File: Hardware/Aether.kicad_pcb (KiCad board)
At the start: 2 copper layers, 70 parts, among them J1 PRGM, Q1 IRLML6401, U1 ANTENOVA-UB, U2 ADF7012, U3 AAT1217, U4 MCP6L02T, U5 MSP430G2553-PW28, X1 VCXO, X2 CRYSTAL

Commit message: RF routing
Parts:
- moved C17 2.92 mm to (174.0, 108.5), turned to 270 degrees
- moved C13 2.50 mm to (187.0, 106.0)
- moved C15 2.50 mm to (174.0, 106.0)
- moved C16 2.50 mm to (172.5, 106.0)
- moved R5 2.50 mm to (187.0, 108.5)
- moved R7 1.50 mm to (175.5, 106.0)
- moved C23 1.25 mm to (188.8, 100.5)
- moved L7 1.00 mm to (187.5, 102.0)
- moved C3 0.81 mm to (137.7, 102.9)
- moved C22 0.75 mm to (186.2, 100.5)
- moved L4 0.75 mm to (178.8, 100.5)
- moved L1 0.50 mm to (121.5, 110.0)
- moved L5 0.50 mm to (180.0, 102.0)
- moved L6 0.50 mm to (185.0, 102.0)
- moved C6 0.40 mm to (139.6, 115.0)
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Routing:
- net GND: track 0.00 -> 27.6 mm, vias 0 -> 8
- net +3.3V: track 2.18 -> 19.4 mm
- net /Transmitter/CPOut: track 0.00 -> 12.0 mm
- net N-0000035: track 0.00 -> 10.8 mm
- net N-0000050: track 0.00 -> 8.46 mm
- net /Transmitter/VCOIn: track 0.00 -> 8.35 mm, vias 0 -> 2
- net N-0000049: track 0.00 -> 4.92 mm
- net N-0000048: track 0.00 -> 4.13 mm
- net N-0000047: track 0.00 -> 4.01 mm
- net N-0000037: track 0.00 -> 2.92 mm
- net N-0000036: track 0.00 -> 2.92 mm
- net N-0000055: track 0.00 -> 2.90 mm
- net N-0000054: track 0.00 -> 2.90 mm
- net /Transmitter/L2: track 0.00 -> 2.18 mm
- net /Transmitter/L1: track 0.00 -> 2.18 mm
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
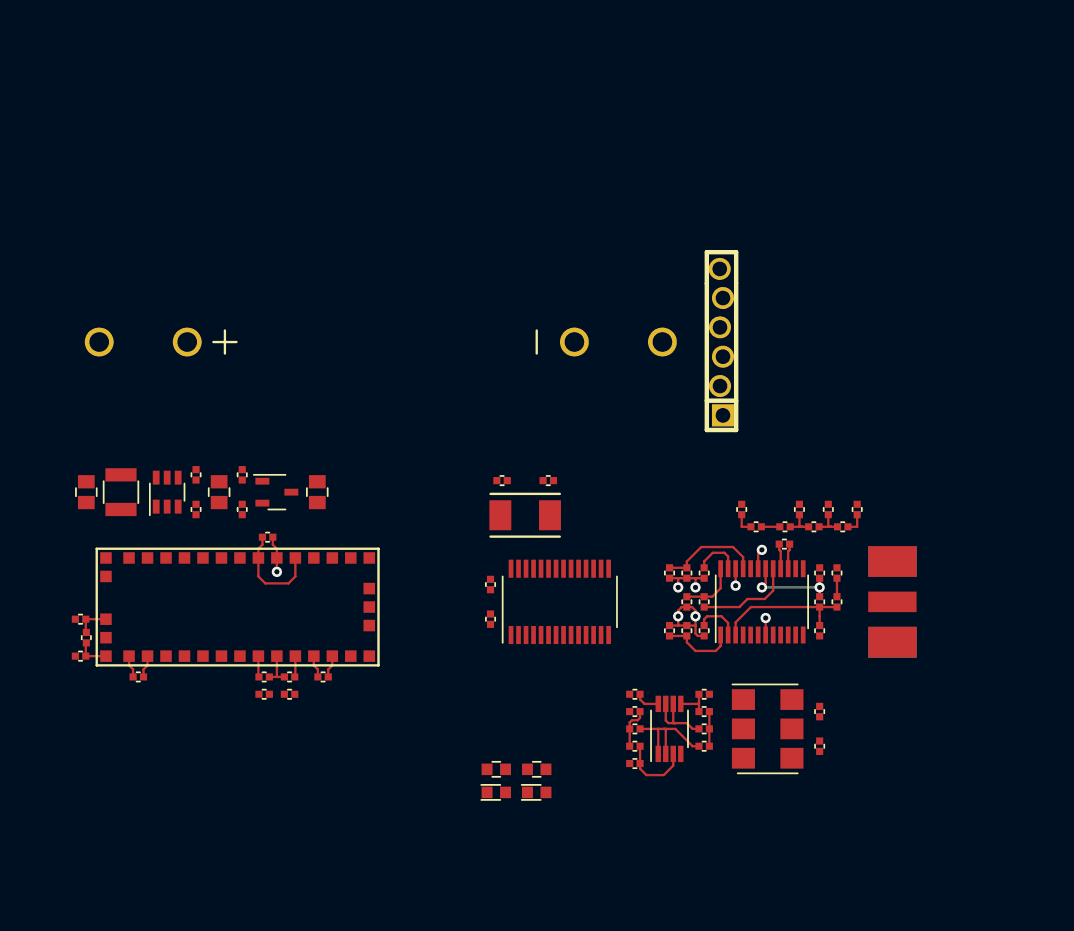
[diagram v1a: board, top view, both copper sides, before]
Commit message: Add expansion headers
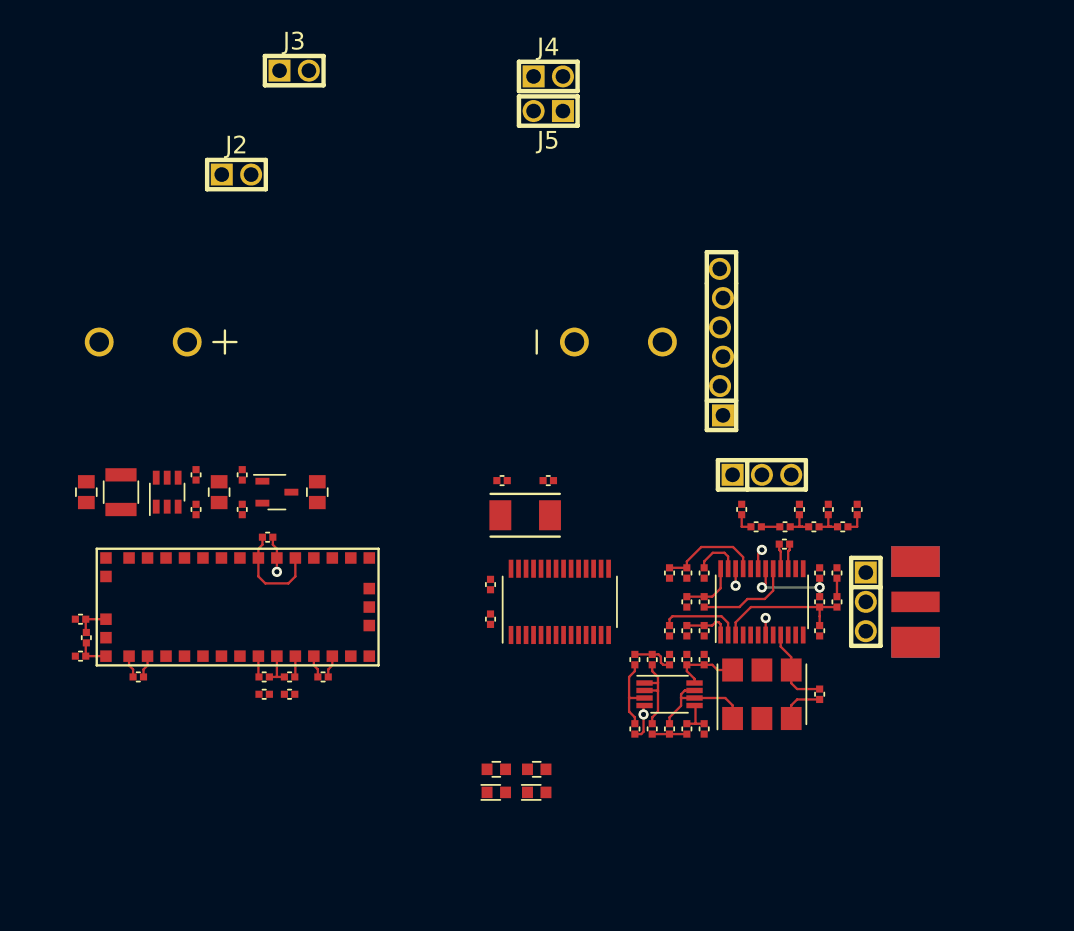
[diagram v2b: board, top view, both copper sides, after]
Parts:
- added J2: CONN-2, HDRV2W38P254_2X1, F.Cu at (135.0, 71.5)
- added J3: CONN-2, HDRV2W38P254_2X1, F.Cu at (140.0, 62.5)
- added J4: CONN-2, HDRV2W38P254_2X1, F.Cu at (162.0, 63.0)
- added J5: CONN-2, HDRV2W38P254_2X1, F.Cu at (162.0, 66.0)
- added J6: CONN-3, HDRV3W38P254_3X1, F.Cu at (180.5, 97.5)
- added J7: CONN-3, HDRV3W38P254_3X1, F.Cu at (189.5, 108.5)
- moved C8 11.0 mm to (175.5, 113.5)
- moved R10 7.50 mm to (169.5, 113.5), turned to 270 degrees
- moved C25 6.18 mm to (171.0, 113.5), turned to 270 degrees
- moved C26 5.41 mm to (174.0, 113.5), turned to 90 degrees
- moved R8 5.41 mm to (172.5, 113.5), turned to 270 degrees
- moved R11 4.74 mm to (171.0, 119.5), turned to 270 degrees
- moved C9 4.50 mm to (185.5, 116.5), turned to 270 degrees
- moved X1 3.04 mm to (180.5, 116.5), turned to 0 degrees
- moved C19 3.00 mm to (172.5, 111.0)
- moved C27 3.00 mm to (169.5, 119.5), turned to 270 degrees
- moved C30 3.00 mm to (172.5, 119.5), turned to 90 degrees
- moved C32 3.00 mm to (175.5, 119.5), turned to 270 degrees
- moved U4 3.00 mm to (172.5, 116.5), turned to 270 degrees
- moved R12 2.12 mm to (174.0, 119.5), turned to 90 degrees
- moved AE1 2.00 mm to (196.0, 108.5)
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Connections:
- AE1 pad P: /Transmitter/RFOut -> N-0000019
- L4 pad 2: (no net) -> +3.3V
- U5 pad 22: (no net) -> /Core/SCL
- X1 pad 2: /Core/TX_En -> (no net)
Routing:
- net N-0000058: track 0.00 -> 7.22 mm
- net GND: track 27.6 -> 21.8 mm, vias 8 -> 5
- net /Core/Mod: track 6.45 -> 10.2 mm
- net N-0000055: track 4.01 -> 7.01 mm
- net N-0000093: track 10.3 -> 7.94 mm
- net +3.3V: track 19.4 -> 20.8 mm
- net N-0000074: track 6.40 -> 6.92 mm

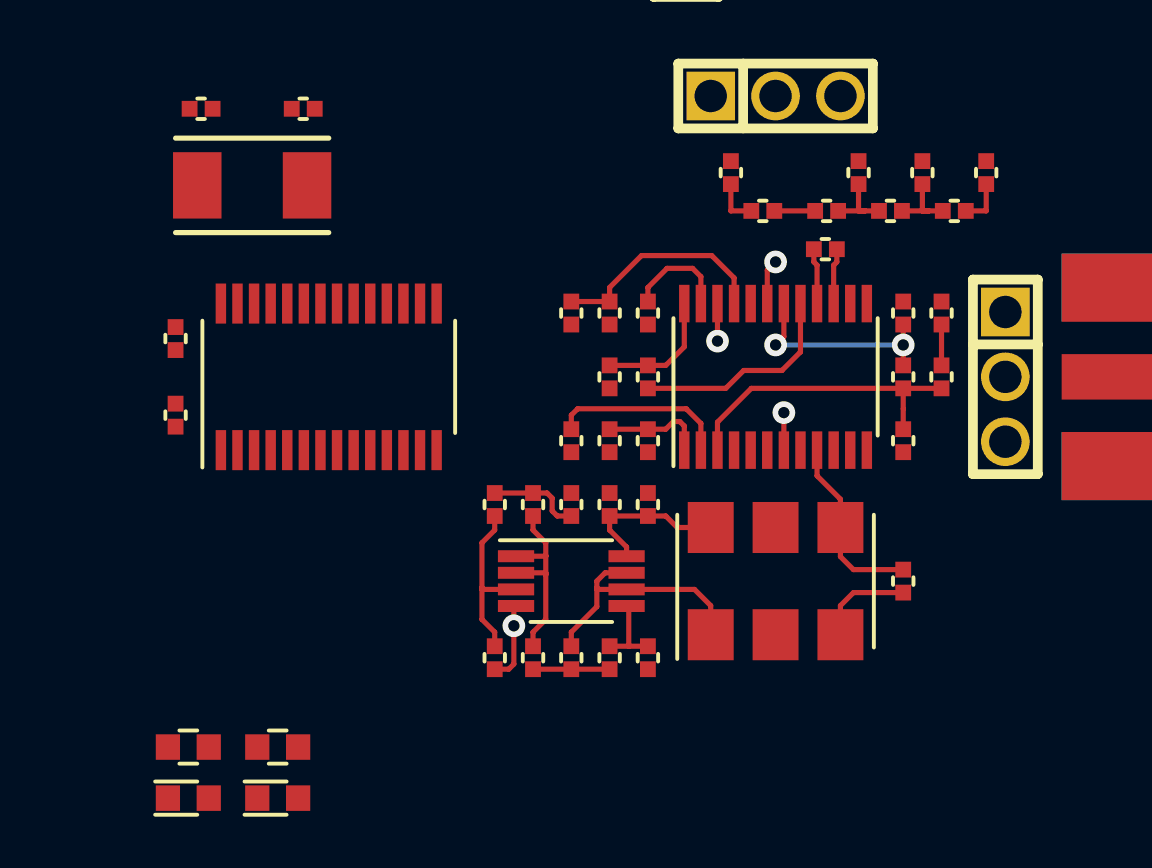
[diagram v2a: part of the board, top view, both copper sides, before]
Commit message: Change to soft SPI, routing
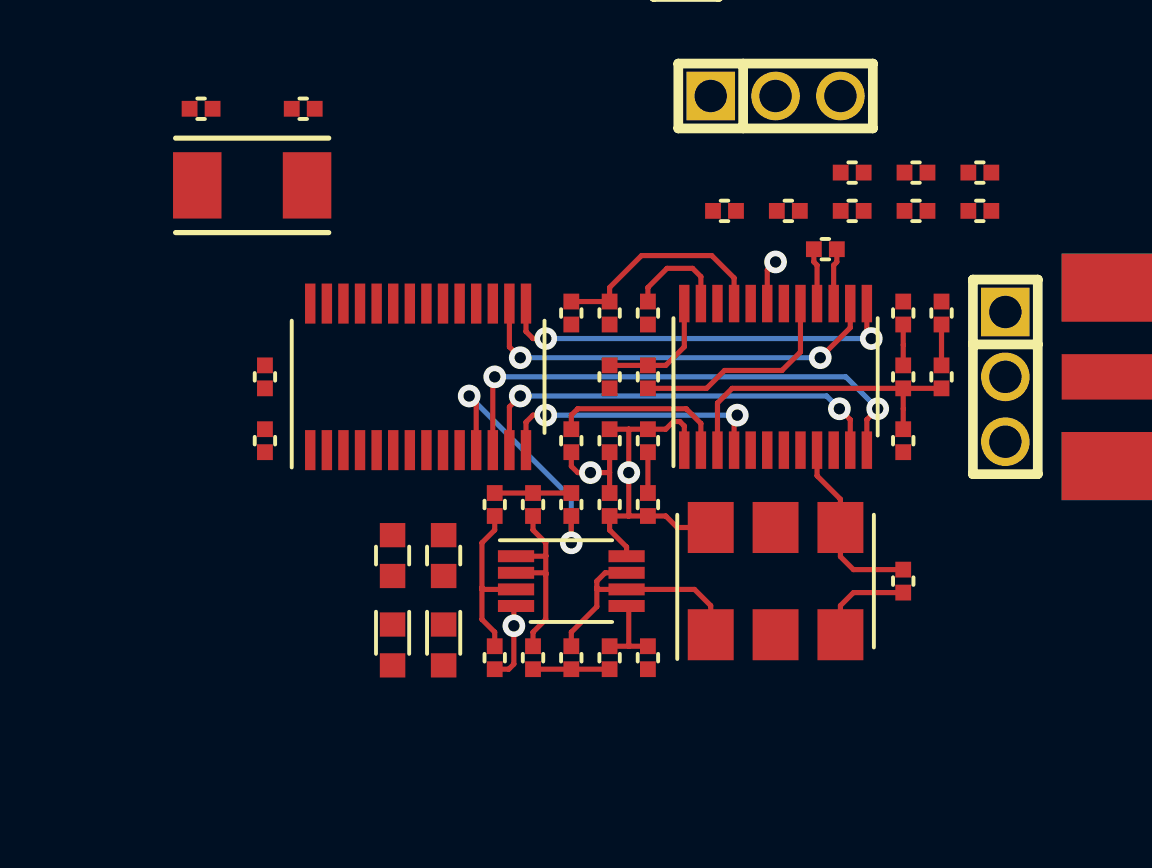
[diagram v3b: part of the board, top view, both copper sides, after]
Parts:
- moved R1 12.5 mm to (167.5, 115.5), turned to 90 degrees
- moved D1 11.7 mm to (167.5, 119.0), turned to 90 degrees
- moved R2 8.75 mm to (165.5, 115.5), turned to 90 degrees
- moved D2 7.50 mm to (165.5, 119.0), turned to 90 degrees
- moved R13 3.81 mm to (160.5, 108.5)
- moved C34 3.64 mm to (160.5, 111.0), turned to 270 degrees
- moved U5 3.50 mm to (166.5, 108.5)
- moved L4 1.52 mm to (178.5, 102.0), turned to 180 degrees
- moved C20 1.00 mm to (183.5, 102.0)
- moved L5 1.00 mm to (181.0, 102.0)
- moved L6 1.00 mm to (186.0, 102.0)
- moved L7 1.00 mm to (188.5, 102.0)
- moved C21 0.25 mm to (183.5, 100.5), turned to 180 degrees
- moved C22 0.25 mm to (186.0, 100.5), turned to 180 degrees
- moved C23 0.25 mm to (188.5, 100.5), turned to 180 degrees
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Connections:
- J1 pad 3: (no net) -> +5V
- J5 pad 1: /Core/SCL -> /Core/SDA
- J5 pad 2: /Core/DATA -> /Core/SCL
- R1 pad 2: (no net) -> /Core/Stat
- R8 pad 1: (no net) -> /Core/AF
- U1 pad 9: (no net) -> /Core/GPS_Perf
- U2 pad 12: /Core/DATA -> /Core/MOSI
- U2 pad 4: (no net) -> /Core/TXD
- U5 pad 10: (no net) -> /Core/CLK_En
- U5 pad 11: (no net) -> /Core/AF
- U5 pad 12: (no net) -> /Core/MOSI
- U5 pad 13: (no net) -> /Core/SCK
- U5 pad 14: (no net) -> /Core/TXD
- U5 pad 15: (no net) -> /Core/SS
- U5 pad 16: (no net) -> /Core/TX_En
- U5 pad 21: (no net) -> +5V
- U5 pad 23: /Core/DATA -> /Core/SDA
- U5 pad 6: /Core/SS -> (no net)
- U5 pad 7: /Core/SCK -> /Core/Stat
- U5 pad 8: (no net) -> /Core/GPS_Perf
- U5 pad 9: (no net) -> /Core/GPS_En
- X1 pad 2: (no net) -> /Core/CLK_En
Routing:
- net /Core/MOSI: track 0.00 -> 20.2 mm, vias 0 -> 2
- net /Core/SCK: track 0.00 -> 16.8 mm, vias 0 -> 2
- net /Core/TX_En: track 0.00 -> 16.7 mm, vias 0 -> 2
- net /Core/SS: track 0.00 -> 16.2 mm, vias 0 -> 2
- net /Core/TXD: track 0.00 -> 10.9 mm, vias 0 -> 2
- net /Core/AF: track 0.00 -> 10.7 mm, vias 0 -> 2
- net /Transmitter/VCOIn: track 8.35 -> 1.60 mm, vias 2 -> 0
- net +3.3V: track 20.8 -> 24.2 mm, vias 0 -> 1
- net N-0000062: track 2.90 -> 0.00 mm
- net N-0000061: track 2.90 -> 0.00 mm
- net GND: track 21.8 -> 24.2 mm, vias 5 -> 4
- net /Transmitter/RFOut: track 1.85 -> 0.00 mm
- net /Transmitter/RF: track 1.85 -> 0.00 mm
- net N-0000063: track 1.60 -> 0.00 mm
- net N-0000079: track 3.67 -> 3.00 mm

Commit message: Additional layout
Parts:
- added R14: 10k, RESC1005-N, F.Cu at (172.5, 102.0)
- B1: footprint BATT-AA-BK92 -> BATT-AA-BK53; moved to B.Cu
- X2: value CRYSTAL -> 8MHz; footprint XTAL-2SMD-60x35 -> XTAL-2SMD-50X32
- moved B1 52.8 mm to (173.5, 132.0)
- moved J5 34.3 mm to (169.5, 99.5), turned to 0 degrees
- moved C1 29.3 mm to (137.5, 128.0)
- moved C24 29.3 mm to (117.5, 128.0)
- moved C28 29.3 mm to (127.0, 129.5)
- moved C29 29.3 mm to (129.0, 128.0)
- moved L8 29.3 mm to (120.5, 128.0)
- moved Q1 29.3 mm to (134.0, 128.0)
- moved R3 29.3 mm to (131.0, 129.5)
- moved R4 29.3 mm to (131.0, 126.5)
- moved R9 29.3 mm to (127.0, 126.5)
- moved U3 29.3 mm to (124.5, 128.0)
- moved J6 6.80 mm to (187.0, 99.5)
- moved J1 5.88 mm to (178.2, 91.8), turned to 180 degrees
- moved C31 4.03 mm to (162.0, 98.5), turned to 180 degrees
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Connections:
- J2 pad 1: (no net) -> +BATT
- J2 pad 2: (no net) -> GND
- J6 pad 1: (no net) -> +BATT
- U5 pad 21: +5V -> N-0000068
- U5 pad 7: /Core/Stat -> /Core/GPS_Perf
- U5 pad 8: /Core/GPS_Perf -> /Core/GPS_En
- U5 pad 9: /Core/GPS_En -> /Core/Stat
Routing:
- net N-0000040: track 10.8 -> 0.00 mm
- net /Core/XOut: track 0.00 -> 9.03 mm
- net /Core/XIn: track 0.00 -> 9.03 mm
- net /Transmitter/VCOIn: track 1.60 -> 9.15 mm, vias 0 -> 2
- net GND: track 24.2 -> 20.0 mm
- net /Core/Stat: track 0.00 -> 3.34 mm
- net N-0000041: track 2.92 -> 0.00 mm
- net N-0000039: track 2.92 -> 0.00 mm
- net N-0000026: track 0.00 -> 1.90 mm
- net N-0000025: track 0.00 -> 1.90 mm
- net N-0000045: track 1.82 -> 0.00 mm
- net N-0000044: track 1.82 -> 0.00 mm
- net /Core/CLK_En: track 0.00 -> 1.79 mm, vias 0 -> 1
- net +3.3V: track 24.2 -> 23.6 mm

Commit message: Additional layout
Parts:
- added C35: 4.7uF, CAPC2012-N, F.Cu at (174.0, 103.5)
- C10: value C -> 0.1uF
- C11, C15: value C -> 5.1pF
- C12: value C -> 1200pF
- C13: value C -> 0.018uF
- C14: value C -> 560pF
- C16: value C -> 10nF
- C17: value C -> 0.47uF
- C18: value C -> 0.022uF
- C19: value C -> 1uF
- C20: value C -> 470pF
- C21, C23: value C -> 3.3pF
- C22: value C -> 8.2pF
- C31, C33: value C -> 22pF
- D1: value LED -> STAT
- D2: value LED -> PWR
- L3: value L -> 19.2nH
- L4, L6, L7: value L -> 22nH
- L5: value L -> 10pF
- R1, R2: value R -> 120
- R5: value R -> 820
- R6: value R -> 1.6k
- R7: value R -> 3.6k
- moved J1 29.0 mm to (158.0, 112.5), turned to 270 degrees
- moved C2 16.9 mm to (132.0, 99.0)
- moved C3 16.9 mm to (143.2, 86.9)
- moved C4 16.9 mm to (142.9, 99.0)
- moved C5 16.9 mm to (148.0, 99.0)
- moved C6 16.9 mm to (145.1, 99.0)
- moved C7 16.9 mm to (127.5, 95.6)
- moved FB1 16.9 mm to (142.9, 100.5)
- moved FB2 16.9 mm to (145.1, 100.5)
- moved L1 16.9 mm to (127.0, 94.0)
- moved L2 16.9 mm to (127.0, 97.2)
- moved U1 16.9 mm to (128.5, 88.0)
- moved J6 7.50 mm to (179.5, 99.5)
- moved R14 4.07 mm to (168.5, 102.8)
- moved C21 3.26 mm to (184.5, 100.2), turned to 90 degrees
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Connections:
- U5 pad 10: /Core/CLK_En -> /Core/AF
- U5 pad 11: /Core/AF -> /Core/CLK_En
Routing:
- net GND: track 20.0 -> 35.4 mm, vias 4 -> 6
- net /Transmitter/RF: track 0.00 -> 5.26 mm
- net /Transmitter/RFOut: track 0.00 -> 4.56 mm
- net N-0000017: track 0.00 -> 3.80 mm
- net N-0000048: track 0.00 -> 2.90 mm
- net N-0000047: track 0.00 -> 2.90 mm
- net /Core/AF: track 10.7 -> 8.31 mm
- net N-0000049: track 0.00 -> 1.60 mm
- net +3.3V: track 23.6 -> 24.2 mm

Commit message: RF layout
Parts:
- B1: footprint BATT-AA-BK53 -> BATT-AA-BK92
- moved J4 54.5 mm to (162.5, 117.5), turned to 270 degrees
- moved C1 33.6 mm to (154.5, 99.0)
- moved C24 33.6 mm to (134.5, 99.0)
- moved C28 33.6 mm to (144.0, 100.5)
- moved C29 33.6 mm to (146.0, 99.0)
- moved L8 33.6 mm to (137.5, 99.0)
- moved Q1 33.6 mm to (151.0, 99.0)
- moved R3 33.6 mm to (148.0, 100.5)
- moved R4 33.6 mm to (148.0, 97.5)
- moved R9 33.6 mm to (144.0, 97.5)
- moved U3 33.6 mm to (141.5, 99.0)
- moved B1 26.9 mm to (168.5, 103.5)
- moved C5 20.9 mm to (152.0, 119.5), turned to 0 degrees
- moved C2 20.7 mm to (134.5, 119.5)
- moved C3 20.7 mm to (145.7, 107.4)
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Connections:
- U5 pad 15: /Core/SS -> /Core/TX_En
- U5 pad 16: /Core/TX_En -> /Core/SS
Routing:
- net GND: track 35.4 -> 93.9 mm, vias 6 -> 20
- net /Core/RX: track 0.00 -> 18.5 mm, vias 0 -> 1
- net +3.3V: track 24.2 -> 33.8 mm
- net /GPS/RX: track 0.00 -> 9.24 mm, vias 0 -> 1
- net /Core/SCL: track 0.00 -> 9.03 mm
- net /Core/SDA: track 0.00 -> 8.25 mm
- net /Core/TX_En: track 16.7 -> 24.9 mm
- net N-0000049: track 1.60 -> 8.31 mm
- net N-0000040: track 0.00 -> 3.89 mm
- net N-0000045: track 0.00 -> 3.12 mm
- net N-0000044: track 0.00 -> 3.12 mm
- net N-0000041: track 0.00 -> 2.92 mm
- net N-0000039: track 0.00 -> 2.92 mm
- net /Core/SS: track 16.7 -> 18.6 mm
- net /Transmitter/RF: track 5.26 -> 6.26 mm
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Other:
- net class Default: via_dia 0.889 -> 0.762; via_drill 0.635 -> 0.381
- rule via_min_drill: 0.508 -> 0.3302
- rule via_min_size: 0.889 -> 0.6858

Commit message: Board configuration
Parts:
- moved J3 40.2 mm to (158.0, 98.5), turned to 270 degrees
- moved J2 19.7 mm to (130.5, 105.5), turned to 270 degrees
- moved R14 15.6 mm to (160.5, 114.0), turned to 90 degrees
- moved C29 11.2 mm to (138.8, 107.5), turned to 180 degrees
- moved C1 9.91 mm to (149.4, 107.5), turned to 0 degrees
- moved R9 8.94 mm to (140.0, 105.5), turned to 180 degrees
- moved C28 8.20 mm to (137.5, 105.5), turned to 180 degrees
- moved Q1 5.41 mm to (148.0, 103.5), turned to 180 degrees
- moved C24 4.93 mm to (138.8, 96.5), turned to 180 degrees
- moved U3 4.85 mm to (138.8, 103.0), turned to 270 degrees
- moved R4 3.02 mm to (149.2, 100.2), turned to 0 degrees
- moved L8 1.27 mm to (138.8, 99.2), turned to 180 degrees
- moved R3 1.27 mm to (146.8, 100.2), turned to 180 degrees
- moved C2 0.71 mm to (135.0, 120.0)
- moved C3 0.71 mm to (146.2, 107.9)
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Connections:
- L8 pad 2: N-0000080 (its old number) -> /Core/Lx
- R14 pad 2: N-0000074 (its old number) -> N-0000067
- U3 pad 1: N-0000080 (its old number) -> /Core/Lx
- U5 pad 2: +BATT -> N-0000067
- U5 pad 21: N-0000074 (its old number) -> (no net)
- U5 pad 5: (no net) -> +BATT
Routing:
- net N-0000040: track 3.89 -> 31.8 mm
- net /Core/CLK_En: track 2.23 -> 19.3 mm, vias 1 -> 2
- net /Core/TDIO/RST: track 0.00 -> 15.8 mm
- net /GPS/RX: track 9.24 -> 22.9 mm, vias 1 -> 2
- net /Core/RX: track 18.5 -> 28.7 mm, vias 1 -> 2
- net /Core/TCK/TEST: track 0.00 -> 7.81 mm
- net GND: track 93.9 -> 100.8 mm, vias 20 -> 28
- net +5V: track 0.00 -> 4.14 mm, vias 0 -> 1
- net N-0000067: track 0.00 -> 4.03 mm
- net N-0000038: track 0.00 -> 2.31 mm
- net +3.3V: track 33.8 -> 36.1 mm
- net /Core/GPS_En: track 0.00 -> 1.60 mm
